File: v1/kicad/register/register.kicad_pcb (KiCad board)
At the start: 2 copper layers, 73 x 46 mm, 5 parts, among them J1 DBUS, J2 BASE, J3 CTRL, U1 74LS173, U2 74LS173

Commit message: progress on kicad implementation
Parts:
- added U3: 74LS244, Package_DIP:DIP-20_W7.62mm_LongPads, F.Cu at (141.5, 104.4)
- J1: value DBUS -> RegisterSocket (active-high reset); footprint Connector_PinSocket_2.54mm:PinSocket_1x08_P2.54mm_Vertical -> LNCPU:RegisterPort; moved to F.Cu
- J2: value BASE -> RegisterCtrl; footprint Connector_PinSocket_2.54mm:PinSocket_1x04_P2.54mm_Vertical -> Connector_PinHeader_2.54mm:PinHeader_1x03_P2.54mm_Vertical; moved to F.Cu
- J3: value CTRL -> ASYNC_{out}; footprint Connector_PinHeader_2.54mm:PinHeader_1x03_P2.54mm_Vertical -> Connector_PinSocket_2.54mm:PinSocket_1x08_P2.54mm_Vertical; moved to F.Cu
- U1, U2: value 74LS173 -> 74HC173; footprint Package_DIP:DIP-16_W7.62mm -> Package_DIP:DIP-16_W7.62mm_LongPads; moved to F.Cu
- moved J2 119.0 mm to (175.0, 112.5), turned to 180 degrees
- moved U2 89.3 mm to (189.8, 91.1)
- moved J3 55.6 mm to (142.1, 77.8), turned to 90 degrees
- moved U1 53.2 mm to (121.6, 90.2)
- moved J1 7.33 mm to (96.0, 108.1), turned to 180 degrees
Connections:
- J1 pad 1: Net-(J1-Pin_1) -> Net-(J1-VCC)
- J1 pad 2: Net-(J1-Pin_2) -> Net-(J1-RST)
- J1 pad 3: Net-(J1-Pin_3) -> Net-(J1-CLK)
- J1 pad 4: Net-(J1-Pin_4) -> Net-(J1-GND)
- J1 pad 5: Net-(J1-Pin_5) -> /DBUS0
- J1 pad 6: Net-(J1-Pin_6) -> /DBUS1
- J1 pad 7: Net-(J1-Pin_7) -> /DBUS2
- J1 pad 8: Net-(J1-Pin_8) -> /DBUS3
- J2 pad 1: Net-(J2-Pin_1) -> Net-(J2-~{EN})
- J2 pad 2: Net-(J2-Pin_2) -> Net-(J2-~{R_{in}})
- J2 pad 3: Net-(J2-Pin_3) -> Net-(J2-~{R_{out}})
- J3 pad 1: Net-(J3-Pin_1) -> /ASYNC0
- J3 pad 2: Net-(J3-Pin_2) -> /ASYNC1
- J3 pad 3: Net-(J3-Pin_3) -> /ASYNC2
- U1 pad 1: Net-(J3-Pin_2) -> Net-(J1-GND)
- U1 pad 10: Net-(J3-Pin_3) -> Net-(J2-~{EN})
- U1 pad 11: Net-(J1-Pin_4) -> /DBUS3
- U1 pad 12: Net-(J1-Pin_3) -> /DBUS2
- U1 pad 13: Net-(J1-Pin_2) -> /DBUS1
- U1 pad 14: Net-(J1-Pin_1) -> /DBUS0
- U1 pad 15: Net-(J2-Pin_1) -> Net-(J1-RST)
- U1 pad 16: Net-(J2-Pin_4) -> Net-(J1-VCC)
- U1 pad 2: Net-(J3-Pin_1) -> Net-(J1-GND)
- U1 pad 3: Net-(J1-Pin_1) -> /ASYNC0
- U1 pad 4: Net-(J1-Pin_2) -> /ASYNC1
- U1 pad 5: Net-(J1-Pin_3) -> /ASYNC2
- U1 pad 6: Net-(J1-Pin_4) -> /ASYNC3
- U1 pad 7: Net-(J2-Pin_2) -> Net-(J1-CLK)
- U1 pad 8: Net-(J2-Pin_3) -> Net-(J1-GND)
- U1 pad 9: Net-(J3-Pin_3) -> Net-(J2-~{R_{in}})
- U2 pad 1: Net-(J3-Pin_2) -> Net-(J1-GND)
- U2 pad 10: Net-(J3-Pin_3) -> Net-(J2-~{EN})
- U2 pad 11: Net-(J1-Pin_8) -> /DBUS7
- U2 pad 12: Net-(J1-Pin_7) -> /DBUS6
- U2 pad 13: Net-(J1-Pin_6) -> /DBUS5
- U2 pad 14: Net-(J1-Pin_5) -> /DBUS4
- U2 pad 15: Net-(J2-Pin_1) -> Net-(J1-RST)
- U2 pad 16: Net-(J2-Pin_4) -> Net-(J1-VCC)
- U2 pad 2: Net-(J3-Pin_1) -> Net-(J1-GND)
- U2 pad 3: Net-(J1-Pin_5) -> /ASYNC4
- U2 pad 4: Net-(J1-Pin_6) -> /ASYNC5
- U2 pad 5: Net-(J1-Pin_7) -> /ASYNC6
- U2 pad 6: Net-(J1-Pin_8) -> /ASYNC7
- U2 pad 7: Net-(J2-Pin_2) -> Net-(J1-CLK)
- U2 pad 8: Net-(J2-Pin_3) -> Net-(J1-GND)
- U2 pad 9: Net-(J3-Pin_3) -> Net-(J2-~{R_{in}})
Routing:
- net Net-(J1-VCC): track 0.00 -> 179.0 mm, vias 0 -> 2
- net Net-(J1-GND): track 0.00 -> 177.3 mm, vias 0 -> 2
- net /ASYNC5: track 0.00 -> 163.2 mm
- net Net-(J2-~{EN}): track 0.00 -> 158.4 mm, vias 0 -> 3
- net Net-(J1-CLK): track 0.00 -> 154.3 mm, vias 0 -> 3
- net /ASYNC6: track 0.00 -> 148.7 mm, vias 0 -> 2
- net /DBUS4: track 0.00 -> 137.7 mm, vias 0 -> 4
- net /DBUS7: track 0.00 -> 134.0 mm, vias 0 -> 3
- net /DBUS6: track 0.00 -> 131.9 mm, vias 0 -> 3
- net /ASYNC4: track 0.00 -> 121.9 mm, vias 0 -> 3
- net /DBUS5: track 0.00 -> 117.0 mm, vias 0 -> 3
- net Net-(J1-RST): track 0.00 -> 114.4 mm, vias 0 -> 2
- net Net-(J2-~{R_{in}}): track 0.00 -> 114.3 mm, vias 0 -> 2
- net /ASYNC7: track 0.00 -> 98.9 mm
- net /ASYNC2: track 0.00 -> 80.0 mm
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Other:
- board size 73 x 46 mm -> 107.2 x 56 mm
- board text removed: "Register"

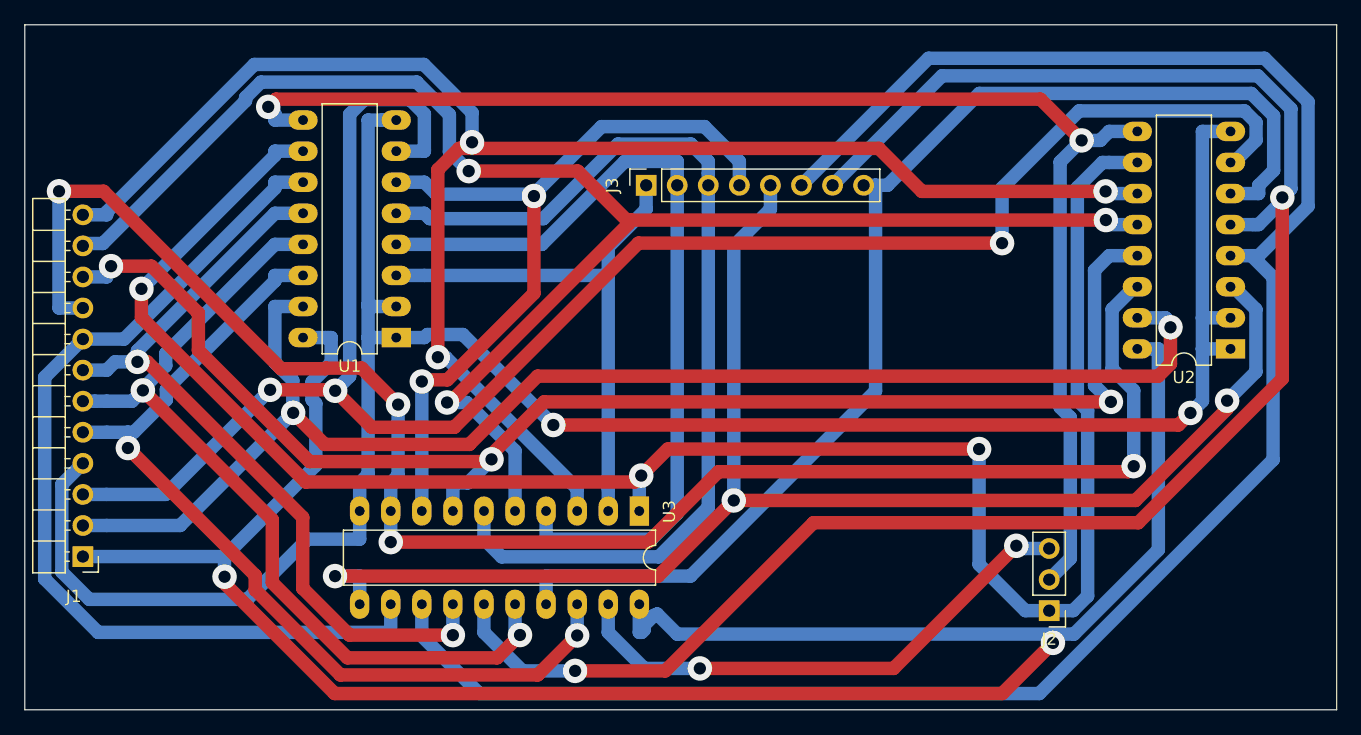
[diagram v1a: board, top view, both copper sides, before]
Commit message: feat: update KiCad files with new pin configurations and error handling improvements
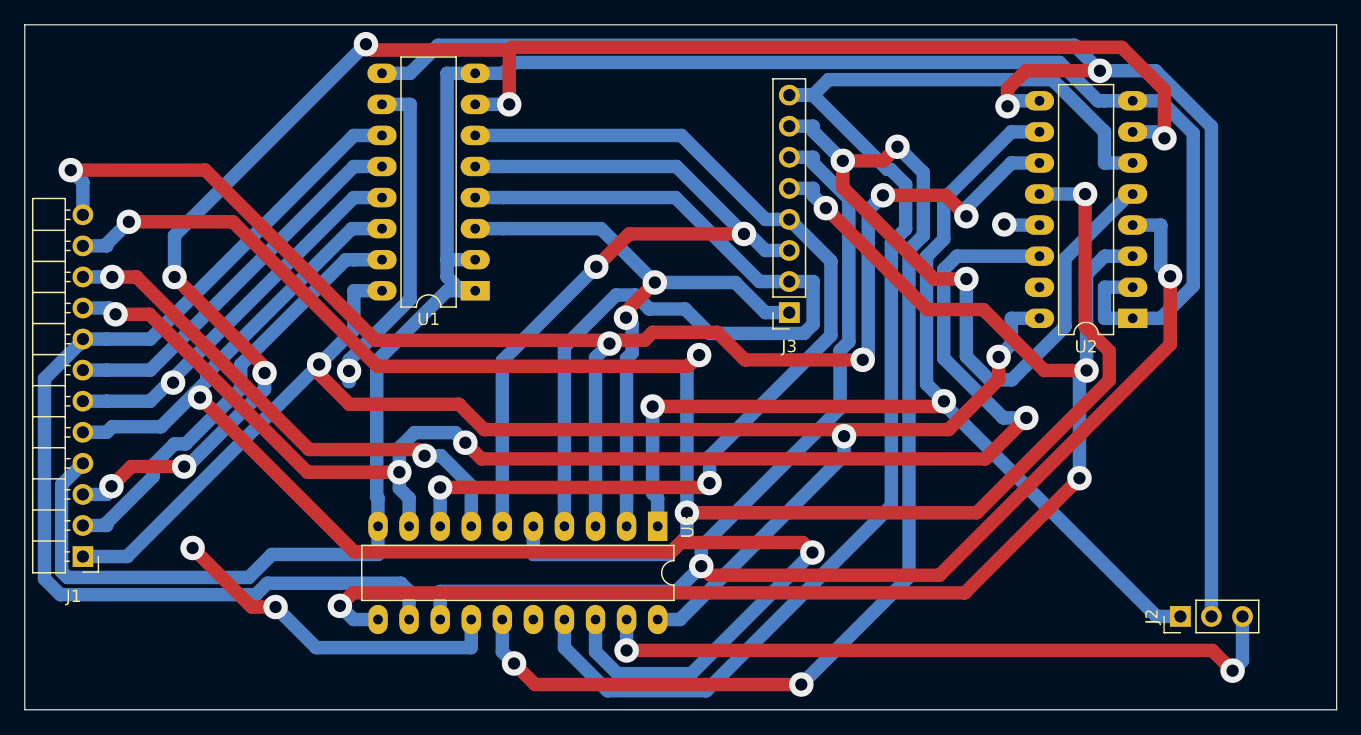
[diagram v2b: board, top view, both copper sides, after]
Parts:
- moved J3 15.7 mm to (153.8, 88.2), turned to 180 degrees
- moved J2 10.7 mm to (185.7, 113.0), turned to 90 degrees
- moved U2 8.38 mm to (181.8, 88.6)
- moved U1 7.50 mm to (128.1, 86.4)
- moved U3 1.95 mm to (143.0, 105.6)
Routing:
- net Net-(J1-RST): track 114.4 -> 35.3 mm, vias 2 -> 0
- net /DBUS5: track 117.0 -> 45.0 mm
- net Net-(J1-VCC): track 179.0 -> 125.9 mm, vias 2 -> 3
- net /DBUS0: track 74.4 -> 118.0 mm
- net Net-(J2-~{EN}): track 158.4 -> 116.4 mm
- net /DBUS1: track 70.4 -> 31.6 mm, vias 2 -> 1
- net /ASYNC5: track 163.2 -> 124.9 mm, vias 0 -> 2
- net /DBUS4: track 137.7 -> 116.5 mm
- net /ASYNC3: track 64.7 -> 82.4 mm
- net Net-(J1-CLK): track 154.3 -> 137.5 mm, vias 3 -> 7
- net /ASYNC6: track 148.7 -> 133.6 mm, vias 2 -> 5
- net /DBUS6: track 131.9 -> 146.0 mm, vias 3 -> 4
- net /ASYNC2: track 80.0 -> 66.1 mm, vias 0 -> 2
- net Net-(J2-~{R_{out}}): track 43.8 -> 57.5 mm
- net /DBUS7: track 134.0 -> 121.3 mm, vias 3 -> 5
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
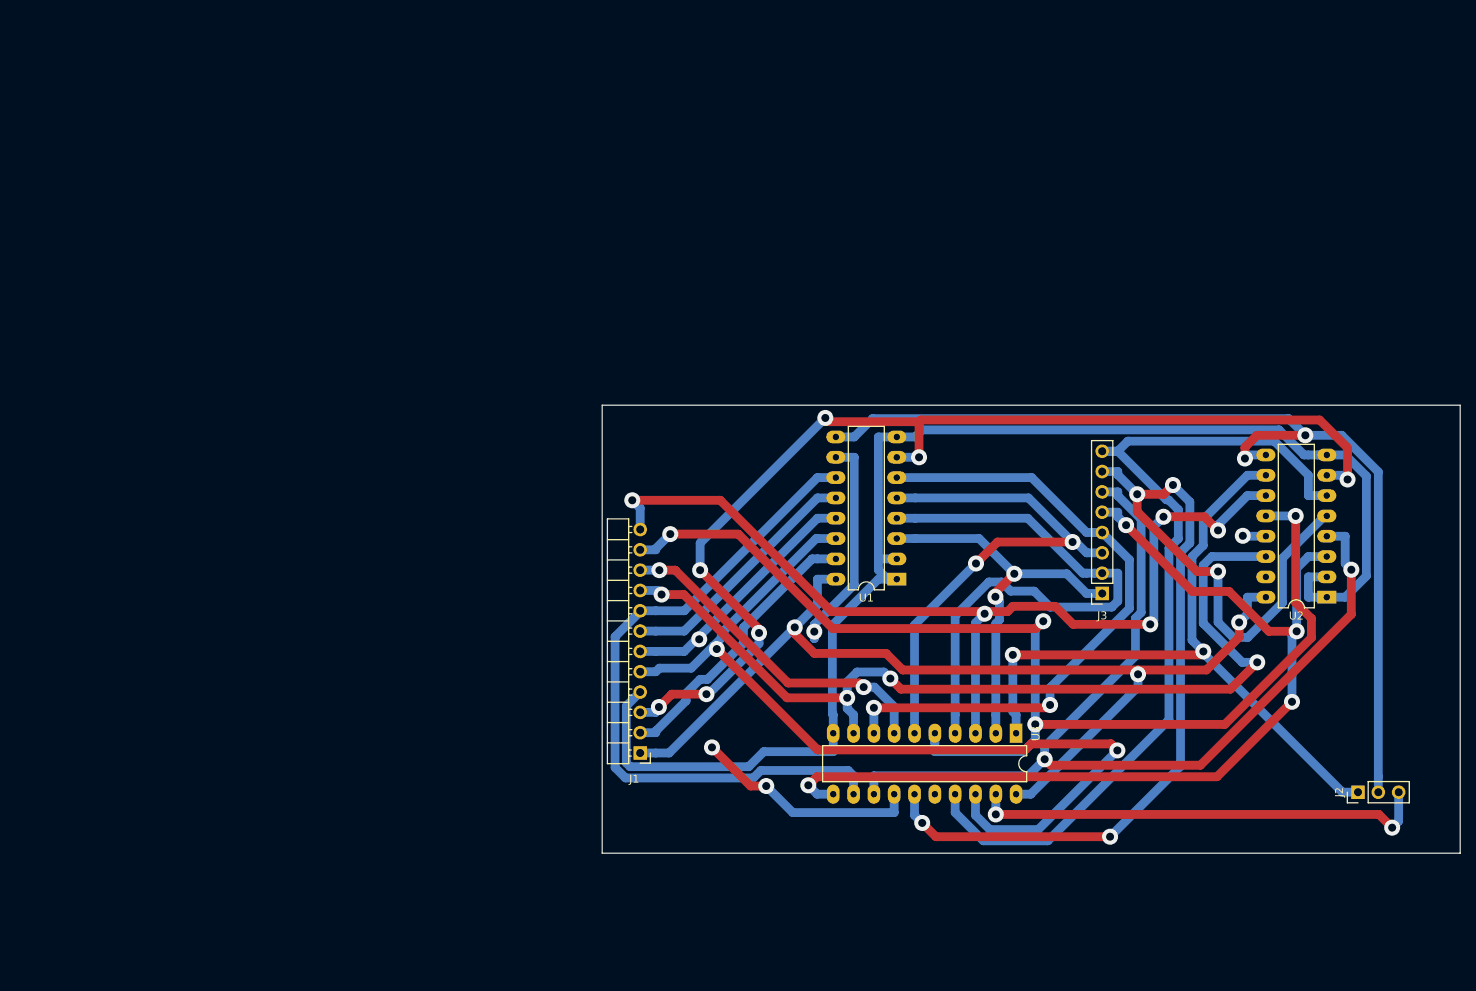
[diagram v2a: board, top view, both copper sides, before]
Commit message: add circuits for AT28C64B loader and register, add v1 components library
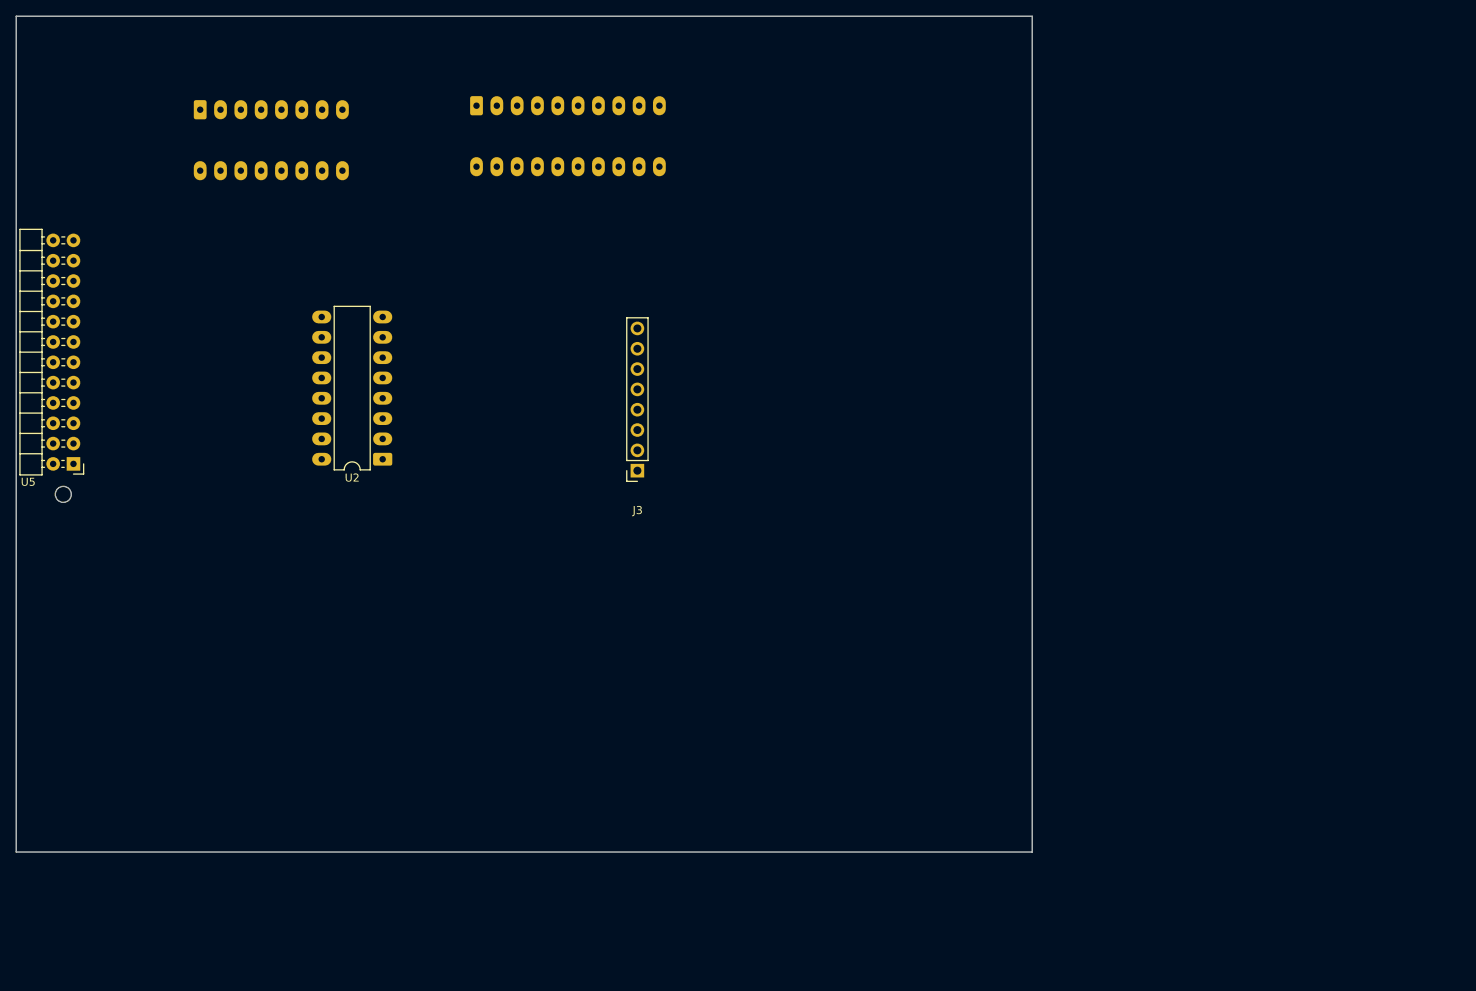
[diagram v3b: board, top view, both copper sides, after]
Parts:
- removed J1: RegisterSocket (active-high reset), LNCPU:RegisterPort
- removed J2: RegisterCtrl, Connector_PinHeader_2.54mm:PinHeader_1x03_P2.54mm_Vertical
- added U5: LNCPU Type B Connector, lncpu:LNCPU_Type_B_Header, F.Cu at (25.2, 72.0)
- U1, U3: moved to B.Cu
- moved U2 119.3 mm to (63.8, 71.4)
- moved U1 105.0 mm to (41.0, 27.7), turned to -90 degrees
- moved U3 103.5 mm to (75.5, 27.2)
- moved J3 60.1 mm to (95.7, 72.8)
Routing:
- net Net-(U1-GND): track 172.7 -> 0.00 mm
- net /DBUS6: track 146.0 -> 0.00 mm, vias 4 -> 0
- net Net-(U1-Cp): track 137.5 -> 0.00 mm, vias 7 -> 0
- net /ASYNC6: track 133.6 -> 0.00 mm, vias 5 -> 0
- net Net-(U1-VCC): track 125.9 -> 0.00 mm, vias 3 -> 0
- net /ASYNC5: track 124.9 -> 0.00 mm, vias 2 -> 0
- net Net-(U1-E1): track 124.0 -> 0.00 mm, vias 2 -> 0
- net /DBUS7: track 121.3 -> 0.00 mm, vias 5 -> 0
- net /ASYNC4: track 120.5 -> 0.00 mm, vias 4 -> 0
- net /DBUS0: track 118.0 -> 0.00 mm, vias 2 -> 0
- net /DBUS4: track 116.5 -> 0.00 mm, vias 4 -> 0
- net Net-(U1-E2): track 116.4 -> 0.00 mm, vias 3 -> 0
- net /ASYNC7: track 109.0 -> 0.00 mm
- net /DBUS3: track 85.7 -> 0.00 mm
- net /ASYNC3: track 82.4 -> 0.00 mm, vias 2 -> 0
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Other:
- board size 107.2 x 56 mm -> 127 x 104.5 mm

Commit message: partial
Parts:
- U1, U3: moved to F.Cu
- moved U1 66.0 mm to (101.5, 54.0), turned to 180 degrees
- moved U2 42.1 mm to (100.3, 92.4)
- moved U5 37.0 mm to (47.0, 42.2), turned to 90 degrees
- moved U3 34.8 mm to (70.9, 61.7)
- moved J3 10.9 mm to (89.9, 63.5), turned to 90 degrees
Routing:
- net Net-(U1-GND): track 0.00 -> 227.8 mm, vias 0 -> 7
- net /DBUS4: track 0.00 -> 130.8 mm, vias 0 -> 5
- net Net-(U1-VCC): track 0.00 -> 129.5 mm, vias 0 -> 4
- net /DBUS3: track 0.00 -> 126.8 mm, vias 0 -> 2
- net /DBUS0: track 0.00 -> 122.7 mm, vias 0 -> 2
- net Net-(U1-E1): track 0.00 -> 120.3 mm, vias 0 -> 3
- net /DBUS2: track 0.00 -> 117.5 mm
- net /ASYNC7: track 0.00 -> 116.3 mm, vias 0 -> 3
- net /DBUS1: track 0.00 -> 115.1 mm, vias 0 -> 2
- net /DBUS5: track 0.00 -> 106.2 mm, vias 0 -> 4
- net Net-(U1-Cp): track 0.00 -> 105.2 mm, vias 0 -> 3
- net Net-(U1-E2): track 0.00 -> 101.9 mm, vias 0 -> 4
- net /DBUS6: track 0.00 -> 98.4 mm, vias 0 -> 4
- net /ASYNC4: track 0.00 -> 97.5 mm, vias 0 -> 3
- net /ASYNC2: track 0.00 -> 87.8 mm, vias 0 -> 2
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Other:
- board size 127 x 104.5 mm -> 78.5 x 66.5 mm
